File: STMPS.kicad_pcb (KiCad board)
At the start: 2 copper layers, 0 parts

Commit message: Fix jumper names for steppers. Start prepping for layout.
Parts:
- added C101: 100uf, Capacitors_SMD:c_elec_6.3x5.8, F.Cu at (163.1, 123.8)
- added C102: 10uf, Capacitors_SMD:C_0805_HandSoldering, F.Cu at (229.9, 94.0)
- added C103: 20pf, Capacitors_SMD:C_0805_HandSoldering, F.Cu at (226.2, 87.6)
- added C104: 20pf, Capacitors_SMD:C_0805_HandSoldering, F.Cu at (204.3, 107.7)
- added C105: 100nf, Capacitors_SMD:C_0805_HandSoldering, F.Cu at (185.7, 64.9)
- added C106: 100nf, Capacitors_SMD:C_0805_HandSoldering, F.Cu at (185.7, 63.0)
- added C107: 100nf, Capacitors_SMD:C_0805_HandSoldering, F.Cu at (185.7, 61.2)
- added C108: 100nf, Capacitors_SMD:C_0805_HandSoldering, F.Cu at (194.9, 53.1)
- added C109: 1uf, Capacitors_SMD:C_0805_HandSoldering, F.Cu at (203.6, 44.8)
- added C110: 100nf, Capacitors_SMD:C_0805_HandSoldering, F.Cu at (198.4, 67.8)
- added C111: 100nf, Capacitors_SMD:C_0805_HandSoldering, F.Cu at (193.0, 71.1)
- added C112: 100nf, Capacitors_SMD:C_0805_HandSoldering, F.Cu at (191.0, 66.6)
- added C113: 4.7uf, Capacitors_SMD:C_0805_HandSoldering, F.Cu at (205.2, 52.9)
- added C114: 4.7uf, Capacitors_SMD:C_0805_HandSoldering, F.Cu at (198.8, 59.5)
- added C115: 0.1uf, Capacitors_SMD:C_0805_HandSoldering, F.Cu at (192.3, 122.1)
- added C116: 10uf, Capacitors_SMD:C_0805_HandSoldering, F.Cu at (219.4, 94.0)
- added C117: 10uf, Capacitors_SMD:C_0805_HandSoldering, F.Cu at (210.8, 100.6)
- added C118: 0.1uf, Capacitors_SMD:C_0805_HandSoldering, F.Cu at (187.2, 122.1)
- added C201: 0.1uf, Capacitors_SMD:C_0805_HandSoldering, F.Cu at (163.8, 181.4)
- added C202: 0.1uf, Capacitors_SMD:C_0805_HandSoldering, F.Cu at (179.6, 181.6)
- added C203: 100uf, Capacitors_SMD:c_elec_6.3x5.8, F.Cu at (179.1, 172.9)
- added C301: 0.1uf, Capacitors_SMD:C_0805_HandSoldering, F.Cu at (227.3, 157.0)
- added C302: 0.1uf, Capacitors_SMD:C_0805_HandSoldering, F.Cu at (239.6, 139.5)
- added C303: 100uf, Capacitors_SMD:c_elec_6.3x5.8, F.Cu at (231.9, 141.8)
- added C401: 0.1uf, Capacitors_SMD:C_0805_HandSoldering, F.Cu at (329.5, 87.6)
- added C402: 0.1uf, Capacitors_SMD:C_0805_HandSoldering, F.Cu at (317.1, 105.1)
- added C403: 100uf, Capacitors_SMD:c_elec_6.3x5.8, F.Cu at (321.8, 90.0)
- added C501: 0.1uf, Capacitors_SMD:C_0805_HandSoldering, F.Cu at (221.7, 177.7)
- added C502: 0.1uf, Capacitors_SMD:C_0805_HandSoldering, F.Cu at (216.6, 177.7)
- added C503: 100uf, Capacitors_SMD:c_elec_6.3x5.8, F.Cu at (231.9, 169.1)
- added D101: 12v_PWR, LEDs:LED_0805, F.Cu at (181.0, 121.1)
- added D102: 3v_PWR, LEDs:LED_0805, F.Cu at (203.4, 120.1)
- added D601: D_Schottky_Small, Diodes_SMD:SOD-123, F.Cu at (244.1, 118.5)
- added D701: r, LEDs:LED_0805, F.Cu at (187.2, 139.1)
- added D801: r, LEDs:LED_0805, F.Cu at (277.1, 87.3)
- added JP101: JUMPER, stmps:MADW__SMD-solder-bridge-narrow, F.Cu at (179.9, 103.6)
- added JP201: MS3, stmps:MADW__SMD-solder-bridge-narrow, F.Cu at (154.3, 185.9)
- added JP202: MS2, stmps:MADW__SMD-solder-bridge-narrow, F.Cu at (167.0, 169.9)
- added JP203: MS1, stmps:MADW__SMD-solder-bridge-narrow, F.Cu at (167.0, 175.4)
- added JP301: MS3, stmps:MADW__SMD-solder-bridge-narrow, F.Cu at (219.8, 144.3)
- added JP302: MS2, stmps:MADW__SMD-solder-bridge-narrow, F.Cu at (219.8, 138.9)
- added JP303: MS1, stmps:MADW__SMD-solder-bridge-narrow, F.Cu at (207.0, 154.8)
- added JP401: MS3, stmps:MADW__SMD-solder-bridge-narrow, F.Cu at (296.9, 103.0)
- added JP402: MS2, stmps:MADW__SMD-solder-bridge-narrow, F.Cu at (309.7, 92.4)
- added JP403: MS1, stmps:MADW__SMD-solder-bridge-narrow, F.Cu at (309.7, 87.0)
- added JP501: MS3, stmps:MADW__SMD-solder-bridge-narrow, F.Cu at (207.0, 182.1)
- added JP502: MS2, stmps:MADW__SMD-solder-bridge-narrow, F.Cu at (219.8, 166.2)
- added JP503: MS1, stmps:MADW__SMD-solder-bridge-narrow, F.Cu at (219.8, 171.6)
- added P101: 12v IN, stmps:5EHDRC_1x04, F.Cu at (158.6, 99.5)
- added P102: 12v, Pin_Headers:Pin_Header_Straight_2x03, F.Cu at (172.1, 107.2)
- added P103: USB_OTG, Connect:USB_Micro-B, F.Cu at (182.3, 112.3)
- added P104: E0_THERM, Pin_Headers:Pin_Header_Straight_1x02, F.Cu at (198.1, 90.6)
- added P105: X_STOP, Pin_Headers:Pin_Header_Straight_1x03, F.Cu at (154.9, 111.1)
- added P106: SWD, Pin_Headers:Pin_Header_Straight_1x06, F.Cu at (149.6, 111.1)
- added P107: BED_THERM, Pin_Headers:Pin_Header_Straight_1x02, F.Cu at (172.8, 120.6)
- added P108: Y_STOP, Pin_Headers:Pin_Header_Straight_1x03, F.Cu at (161.0, 111.1)
- added P109: Z_STOP, Pin_Headers:Pin_Header_Straight_1x03, F.Cu at (154.9, 124.5)
- added P201: MOT, Pin_Headers:Pin_Header_Straight_1x04, F.Cu at (149.6, 173.5)
- added P301: MOT, Pin_Headers:Pin_Header_Straight_1x04, F.Cu at (202.3, 142.5)
- added P401: MOT, Pin_Headers:Pin_Header_Straight_1x04, F.Cu at (292.2, 90.6)
- added P501: MOT, Pin_Headers:Pin_Header_Straight_1x04, F.Cu at (202.3, 169.8)
- added P601: LP_OUT, Pin_Headers:Pin_Header_Straight_1x02, F.Cu at (254.0, 121.6)
- added P701: OUT, stmps:TB-1x02, F.Cu at (157.8, 149.7)
- added P801: OUT, stmps:TB-1x02, F.Cu at (247.7, 97.8)
- added Q601: SSM3K333, TO_SOT_Packages_SMD:SOT-23_Handsoldering, F.Cu at (241.5, 126.6)
- added Q701: IPP039N04L, TO_SOT_Packages_THT:TO-220_Neutral123_Vertical, F.Cu at (174.0, 142.5)
- added Q801: IPP039N04L, TO_SOT_Packages_THT:TO-220_Neutral123_Vertical, F.Cu at (263.8, 90.6)
- added R101: 560, Resistors_SMD:R_0805_HandSoldering, F.Cu at (231.4, 87.6)
- added R102: 56, Resistors_SMD:R_0805_HandSoldering, F.Cu at (197.6, 120.5)
- added R103: 220, Resistors_SMD:R_0805_HandSoldering, F.Cu at (224.7, 94.0)
- added R104: 100k, Resistors_SMD:R_0805_HandSoldering, F.Cu at (190.6, 128.5)
- added R105: 4.7k, Resistors_SMD:R_0805_HandSoldering, F.Cu at (180.1, 127.1)
- added R106: 4.7k, Resistors_SMD:R_0805_HandSoldering, F.Cu at (221.2, 100.4)
- added R107: 4.7k, Resistors_SMD:R_0805_HandSoldering, F.Cu at (214.7, 107.0)
- added R108: 4.7k, Resistors_SMD:R_0805_HandSoldering, F.Cu at (206.9, 114.1)
- added R201: 20k, Resistors_SMD:R_0805_HandSoldering, F.Cu at (169.0, 181.4)
- added R202: 100k, Resistors_SMD:R_0805_HandSoldering, F.Cu at (163.9, 187.8)
- added R203: 100k, Resistors_SMD:R_0805_HandSoldering, F.Cu at (174.4, 181.6)
- added R204: 0.05, Resistors_SMD:R_0805_HandSoldering, F.Cu at (186.9, 170.5)
- added R205: 0.05, Resistors_SMD:R_0805_HandSoldering, F.Cu at (169.2, 188.0)
- added R301: 20k, Resistors_SMD:R_0805_HandSoldering, F.Cu at (227.4, 150.6)
- added R302: 100k, Resistors_SMD:R_0805_HandSoldering, F.Cu at (216.7, 156.8)
- added R303: 100k, Resistors_SMD:R_0805_HandSoldering, F.Cu at (222.0, 150.4)
- added R304: 0.05, Resistors_SMD:R_0805_HandSoldering, F.Cu at (216.7, 150.4)
- added R305: 0.05, Resistors_SMD:R_0805_HandSoldering, F.Cu at (222.0, 156.8)
- added R401: 20k, Resistors_SMD:R_0805_HandSoldering, F.Cu at (311.9, 104.9)
- added R402: 100k, Resistors_SMD:R_0805_HandSoldering, F.Cu at (317.2, 98.7)
- added R403: 100k, Resistors_SMD:R_0805_HandSoldering, F.Cu at (306.5, 104.9)
- added R404: 0.05, Resistors_SMD:R_0805_HandSoldering, F.Cu at (306.5, 98.5)
- added R405: 0.05, Resistors_SMD:R_0805_HandSoldering, F.Cu at (311.9, 98.5)
- added R501: 20k, Resistors_SMD:R_0805_HandSoldering, F.Cu at (216.7, 184.1)
- added R502: 100k, Resistors_SMD:R_0805_HandSoldering, F.Cu at (227.0, 177.9)
- added R503: 100k, Resistors_SMD:R_0805_HandSoldering, F.Cu at (239.7, 166.8)
- added R504: 0.05, Resistors_SMD:R_0805_HandSoldering, F.Cu at (222.0, 184.3)
- added R505: 0.05, Resistors_SMD:R_0805_HandSoldering, F.Cu at (232.3, 177.9)
- added R601: 100k, Resistors_SMD:R_0805_HandSoldering, F.Cu at (259.7, 118.6)
- added R701: 100k, Resistors_SMD:R_0805_HandSoldering, F.Cu at (171.0, 150.6)
- added R702: 100, Resistors_SMD:R_0805_HandSoldering, F.Cu at (182.3, 139.5)
- added R703: 560, Resistors_SMD:R_0805_HandSoldering, F.Cu at (171.0, 157.0)
- added R801: 100k, Resistors_SMD:R_0805_HandSoldering, F.Cu at (260.9, 98.7)
- added R802: 100, Resistors_SMD:R_0805_HandSoldering, F.Cu at (260.9, 105.1)
- added R803: 560, Resistors_SMD:R_0805_HandSoldering, F.Cu at (272.2, 87.6)
- added RV201: 100k, stmps:BOURNS-TC33X-2, F.Cu at (186.8, 176.5)
- added RV301: 100k, stmps:BOURNS-TC33X-2, F.Cu at (232.6, 150.1)
- added RV401: 100k, stmps:BOURNS-TC33X-2, F.Cu at (322.5, 98.2)
- added RV501: 100k, stmps:BOURNS-TC33X-2, F.Cu at (239.6, 172.7)
- added SW101: RST, Buttons_Switches_ThroughHole:SW_PUSH_SMALL, F.Cu at (207.0, 88.5)
- added U101: AOZ8904, TO_SOT_Packages_SMD:SOT-23-6_Handsoldering, F.Cu at (171.9, 129.3)
- added U102: LM1117-3.3v, TO_SOT_Packages_SMD:TO-252-2Lead, F.Cu at (188.7, 95.9)
- added U103: STM32F411RCTx, Housings_QFP:LQFP-64_10x10mm_Pitch0.5mm, F.Cu at (173.0, 70.6)
- added U104: M24C04, Housings_SOIC:SOIC-8_3.9x4.9mm_Pitch1.27mm, F.Cu at (199.0, 99.9)
- added U201: A5984, stmps:TSSOP-24_4.4x7.8mm_Pitch0.65mm, F.Cu at (156.0, 173.4)
- added U301: A5984, stmps:TSSOP-24_4.4x7.8mm_Pitch0.65mm, F.Cu at (208.7, 142.3)
- added U401: A5984, stmps:TSSOP-24_4.4x7.8mm_Pitch0.65mm, F.Cu at (298.6, 90.5)
- added U501: A5984, stmps:TSSOP-24_4.4x7.8mm_Pitch0.65mm, F.Cu at (208.7, 169.6)
- added W101: TEST_1P, Connect:PINTST, F.Cu at (190.5, 110.2)
- added W102: TEST_1P, Connect:PINTST, F.Cu at (206.4, 95.0)
- added W103: TEST_1P, Connect:PINTST, F.Cu at (198.4, 106.8)
- added W104: TEST_1P, Connect:PINTST, F.Cu at (215.1, 86.8)
- added Y101: Crystal, Crystals:Crystal_HC49-U_Vertical, F.Cu at (189.1, 102.9)

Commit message: Complete routing, first pass.
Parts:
- removed C115: 0.1uf, Capacitors_SMD:C_0805_HandSoldering
- removed SW101: RST, Buttons_Switches_ThroughHole:SW_PUSH_SMALL
- removed W101, W102, W103, W104: TEST_1P, Connect:PINTST
- added C204: 0.1uf, Capacitors_SMD:C_0805_HandSoldering, F.Cu at (166.9, 126.4)
- added C304: 0.1uf, Capacitors_SMD:C_0805_HandSoldering, F.Cu at (166.6, 143.8)
- added C404: 0.1uf, Capacitors_SMD:C_0805_HandSoldering, F.Cu at (197.6, 126.5)
- added C504: 0.1uf, Capacitors_SMD:C_0805_HandSoldering, F.Cu at (197.6, 143.7)
- C102, C105, C106, C107, C108, C109, C110, C111, C112, C113, C114, R104, R701, R702, R801, R802, U102: moved to B.Cu
- JP101: value JUMPER -> BOOT0; footprint stmps:MADW__SMD-solder-bridge-narrow -> Pin_Headers:Pin_Header_Straight_1x02_Pitch2.00mm
- P701, P801: footprint stmps:TB-1x02 -> Connectors_Molex:Molex_KK-6410-02_02x2.54mm_Straight
- moved C403 171.3 mm to (153.0, 119.4), turned to 90 degrees
- moved C401 170.7 mm to (161.3, 117.0), turned to 270 degrees
- moved RV401 165.2 mm to (159.8, 127.1), turned to 270 degrees
- moved R402 158.8 mm to (159.5, 117.0), turned to 270 degrees
- moved R401 157.8 mm to (155.7, 127.1), turned to 90 degrees
- moved JP402 152.0 mm to (160.4, 120.9), turned to 270 degrees
- moved JP403 151.9 mm to (161.6, 120.9), turned to 270 degrees
- moved C402 150.7 mm to (166.9, 115.9)
- moved R403 147.8 mm to (159.9, 123.6), turned to 180 degrees
- moved R405 139.9 mm to (174.1, 122.8)
- moved JP401 139.0 mm to (159.1, 120.9), turned to 270 degrees
- moved U401 135.3 mm to (166.9, 121.1)
- moved R404 134.1 mm to (174.1, 119.5)
- moved P401 118.5 mm to (178.8, 124.8), turned to 180 degrees
- moved C109 106.9 mm to (141.4, 131.7)
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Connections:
- net Net-(C102-Pad1) renamed /+5v
- U101 pad 1: Net-(U101-Pad1) -> /USB_DP
- U101 pad 3: Net-(U101-Pad3) -> /USB_DN
- U101 pad 4: /USB_DN -> Net-(U101-Pad4)
- U101 pad 6: /USB_DP -> Net-(U101-Pad6)
- U103 pad 33: /E0_Stepper/ENABLE -> /E0_Stepper/STEP
- U103 pad 34: /E0_Stepper/STEP -> /E0_Stepper/DIR
- U103 pad 35: /E0_Stepper/DIR -> /E0_Stepper/ENABLE
- U201 pad 15: Net-(P201-Pad2) -> Net-(P201-Pad1)
- U201 pad 18: Net-(P201-Pad1) -> Net-(P201-Pad2)
- U201 pad T: (no net) -> GND
- U301 pad 15: Net-(P301-Pad2) -> Net-(P301-Pad1)
- U301 pad 18: Net-(P301-Pad1) -> Net-(P301-Pad2)
- U301 pad T: (no net) -> GND
- U401 pad 15: Net-(P401-Pad2) -> Net-(P401-Pad1)
- U401 pad 18: Net-(P401-Pad1) -> Net-(P401-Pad2)
- U401 pad T: (no net) -> GND
- U501 pad 15: Net-(P501-Pad2) -> Net-(P501-Pad1)
- U501 pad 18: Net-(P501-Pad1) -> Net-(P501-Pad2)
- U501 pad T: (no net) -> GND
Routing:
- net +3.3v: track 0.00 -> 248.6 mm, vias 0 -> 9
- net GND: track 0.00 -> 147.1 mm, vias 0 -> 60
- net /BED_FET/PWM_IN: track 0.00 -> 97.7 mm, vias 0 -> 3
- net /E0_FET/PWM_IN: track 0.00 -> 79.3 mm, vias 0 -> 3
- net /Fan_FET/PWM_IN: track 0.00 -> 78.8 mm, vias 0 -> 2
- net /X_Stepper/DIR: track 0.00 -> 74.3 mm, vias 0 -> 2
- net /X_Stepper/ENABLE: track 0.00 -> 71.6 mm, vias 0 -> 3
- net /X_Stepper/STEP: track 0.00 -> 70.2 mm, vias 0 -> 2
- net /E0_Stepper/ENABLE: track 0.00 -> 62.0 mm, vias 0 -> 3
- net /E0_Stepper/DIR: track 0.00 -> 57.0 mm, vias 0 -> 2
- net /E0_Stepper/STEP: track 0.00 -> 53.8 mm, vias 0 -> 2
- net /NRST: track 0.00 -> 51.0 mm, vias 0 -> 1
- net /Y_Stepper/DIR: track 0.00 -> 39.3 mm, vias 0 -> 2
- net /Y_Stepper/STEP: track 0.00 -> 36.7 mm, vias 0 -> 2
- net /Y_Stepper/ENABLE: track 0.00 -> 35.5 mm, vias 0 -> 3
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- added copper zone on F.Cu, net +12v
- added copper zone on B.Cu, net GND
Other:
- board outline added: 98.3 x 37.3 mm
- net class Default: via_dia 0.6858 -> 0.7112
- net class Low-Power added: clearance 0.1524, trace_width 0.254, via_dia 0.7112, via_drill 0.3302
- net class Power: clearance 0.254 -> 0.1524; trace_width 0.6096 -> 0.8128; via_dia 0.889 -> 0.7112; via_drill 0.4572 -> 0.3302

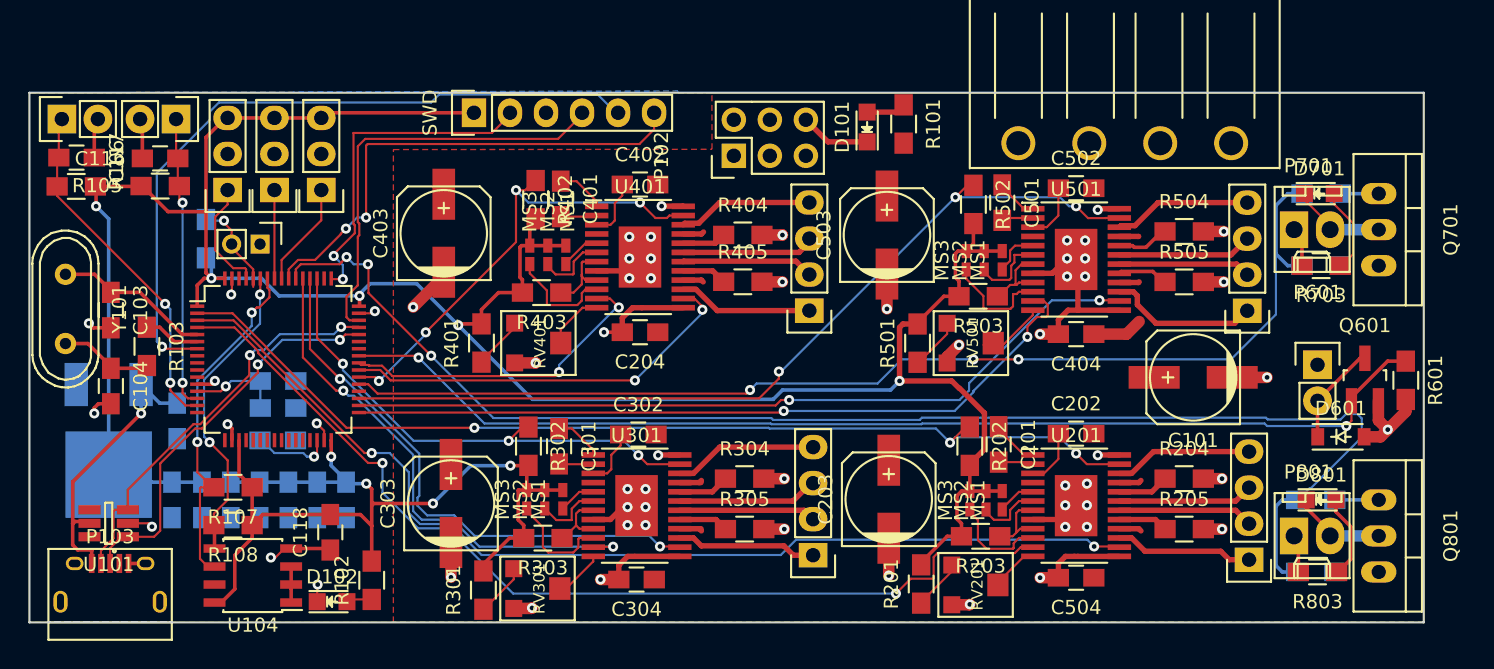
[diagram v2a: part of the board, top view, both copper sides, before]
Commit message: Cleanup silkscreen and other minor tweaks.
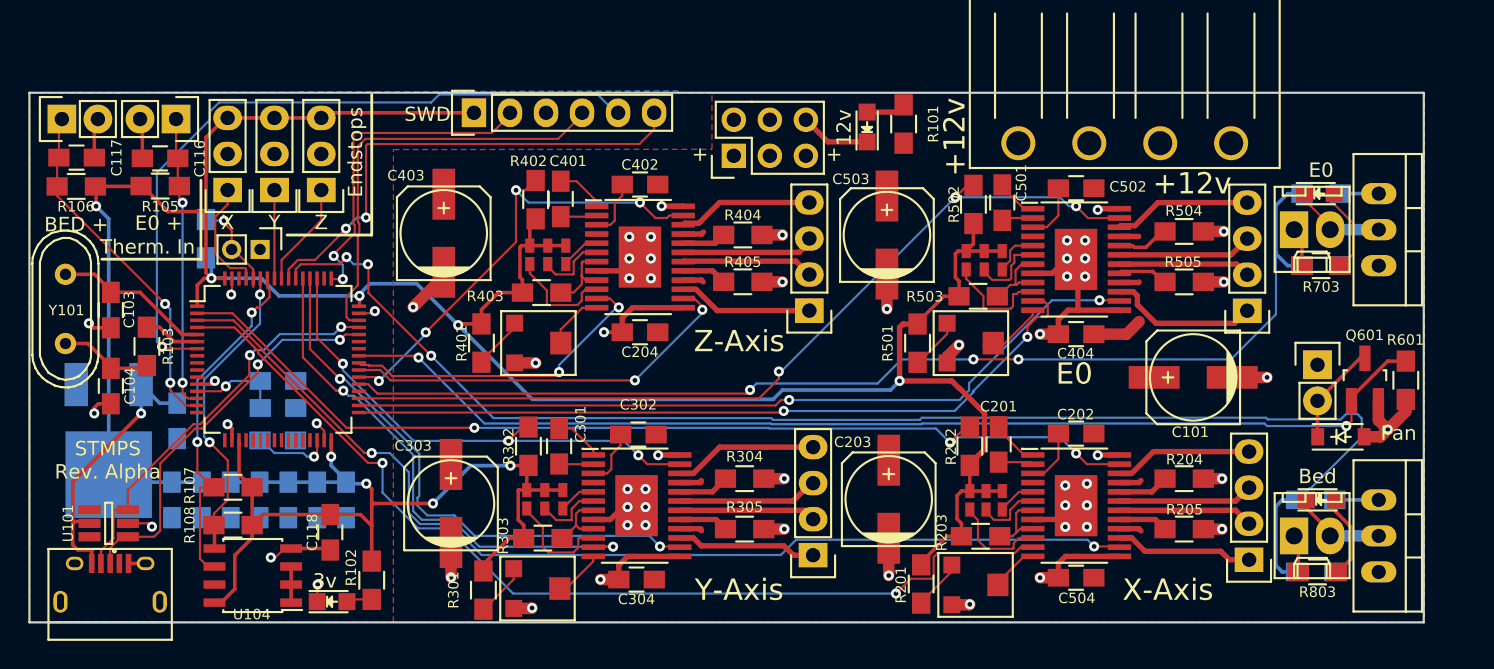
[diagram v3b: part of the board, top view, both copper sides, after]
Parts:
- added REF**: Symbol_OSHW-Logo_SilkScreen, Symbols:Symbol_OSHW-Logo_SilkScreen, B.Cu at (130.3, 118.1)
- JP503: value MS1 -> eMS1
- moved JP101 0.38 mm to (140.1, 120.5)
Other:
- board text added: "+"
- board text added: "+12v"
- board text added: "12v"
- board text added: "3v"
- board text added: "BED +"
- board text added: "Bed"
- board text added: "E0"
- board text added: "E0 +"
- board text added: "Endstops"
- board text added: "Fan"
- board text added: "STMPS Rev. Alpha"
- board text added: "Therm. In"
- board text added: "X"
- board text added: "X-Axis"
- board text added: "Y"
- board text added: "Y-Axis"
- board text added: "Z"
- board text added: "Z-Axis"

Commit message: Finalized layout for Alpha 1.
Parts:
- JP503: value eMS1 -> MS1
- R201, R301, R401, R501: value 20k -> 200k
- R204, R205, R304, R305, R404, R405, R504, R505: value 0.05 -> 0.1
- moved REF** 1.78 mm to (130.3, 116.3), turned to 180 degrees
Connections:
- R201 pad 2: +3.3v -> +12v
- R301 pad 2: +3.3v -> +12v
- R401 pad 2: +3.3v -> +12v
- R501 pad 2: +3.3v -> +12v
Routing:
- net +3.3v: track 248.6 -> 240.4 mm
- net +12v: track 21.7 -> 22.3 mm

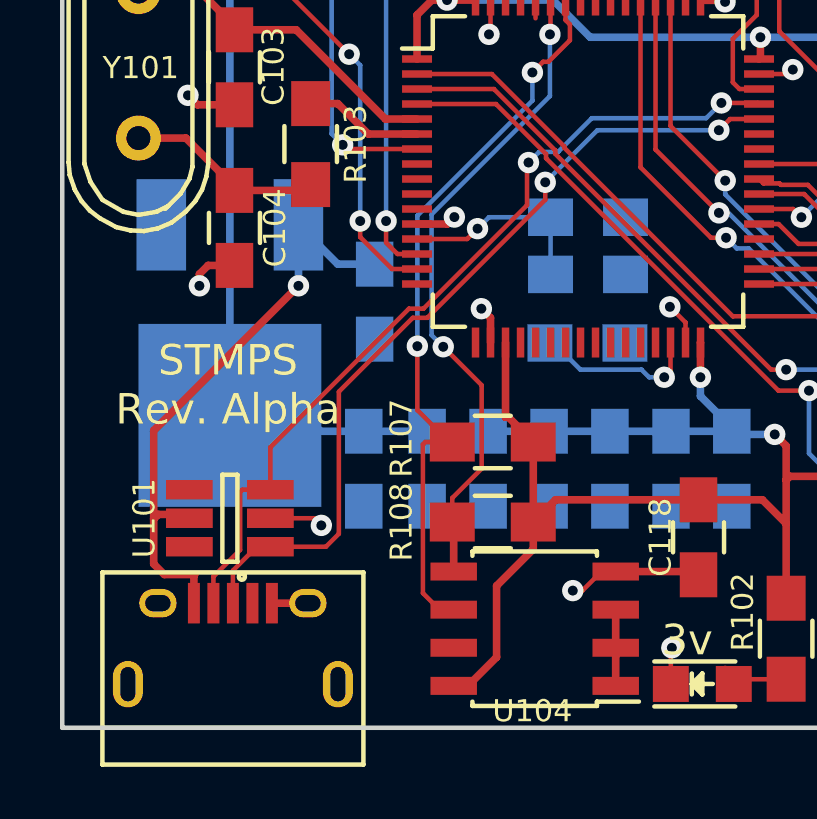
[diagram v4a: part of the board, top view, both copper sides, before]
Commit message: Fix USB connection. Cleanups.
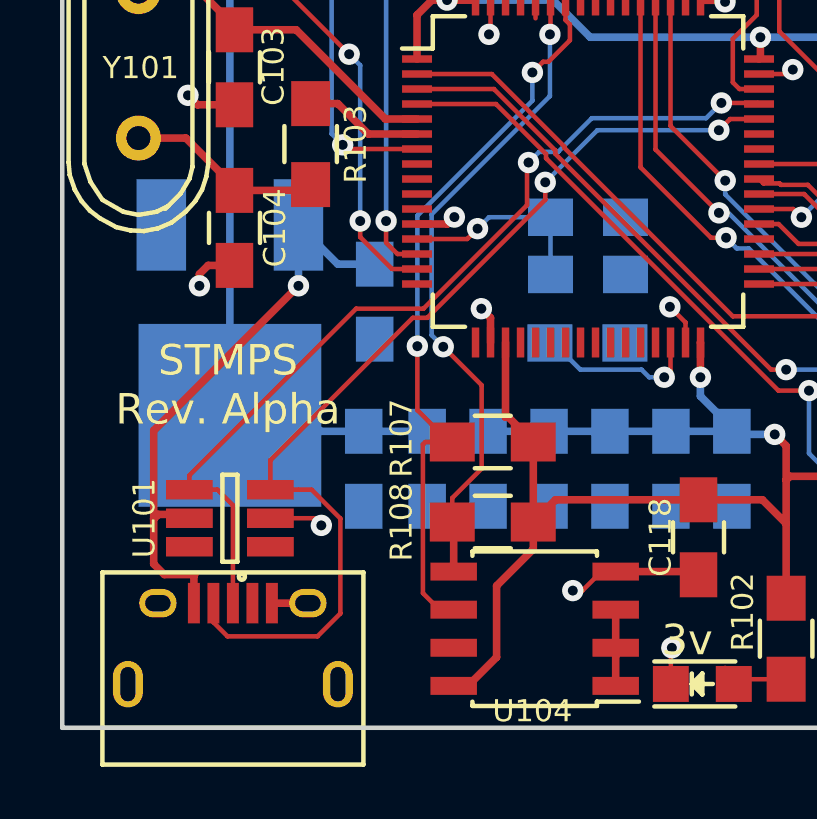
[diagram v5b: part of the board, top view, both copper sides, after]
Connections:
- P103 pad 2: /USB_DN -> /USB_DM
- U101 pad 1: /USB_DP -> Net-(U101-Pad1)
- U101 pad 3: /USB_DN -> /USB_DM
- U101 pad 4: Net-(U101-Pad4) -> /USB_DP
- U103 pad 44: /USB_DP -> /USB_DM
- U103 pad 45: /USB_DN -> /USB_DP
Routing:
- net /USB_DM: track 0.00 -> 33.6 mm, vias 0 -> 2
- net /USB_DN: track 28.4 -> 0.00 mm, vias 2 -> 0
- net /USB_DP: track 28.0 -> 30.4 mm

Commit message: WIP rev B.
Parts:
- removed C118: 0.1uf, Capacitors_SMD:C_0805_HandSoldering
- removed R107, R108: 4.7k, Resistors_SMD:R_0805_HandSoldering
- removed REF**: Symbol_OSHW-Logo_SilkScreen, Symbols:Symbol_OSHW-Logo_SilkScreen
- removed U104: M24C04, Housings_SOIC:SOIC-8_3.9x4.9mm_Pitch1.27mm
- added D103: D_Schottky_Small, Diodes_SMD:SOD-123, F.Cu at (150.4, 182.8)
- added U105: CHIP-TOP, stmps:CHIP-MIN, F.Cu at (47.8, 79.8)
- C103, C104, D701, D801, R103, R703, R803: moved to B.Cu
- moved Q701 91.6 mm to (127.4, 115.3), turned to 90 degrees
- moved D601 89.0 mm to (127.4, 128.8)
- moved R601 89.0 mm to (132.0, 124.8)
- moved P601 89.0 mm to (125.7, 123.7)
- moved Q601 89.0 mm to (129.1, 124.7)
- moved R702 88.2 mm to (126.7, 120.4), turned to 0 degrees
- moved R701 84.8 mm to (130.2, 118.9), turned to 90 degrees
- moved D701 84.6 mm to (130.2, 114.3), turned to 90 degrees
- moved Q801 83.1 mm to (139.7, 115.7), turned to 90 degrees
- moved R703 81.8 mm to (133.5, 113.3), turned to 0 degrees
- moved P701 77.9 mm to (135.1, 116.3), turned to 180 degrees
- moved R802 77.4 mm to (139.2, 120.4), turned to 0 degrees
- moved D801 76.2 mm to (142.5, 114.3), turned to 90 degrees
- moved R801 76.0 mm to (142.5, 118.9), turned to 90 degrees
- moved P301 75.7 mm to (105.9, 122.7), turned to 270 degrees
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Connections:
- U103 pad 10: Net-(U103-Pad10) -> /E0_Stepper/ENABLE
- U103 pad 33: /E0_Stepper/STEP -> Net-(U103-Pad33)
- U103 pad 34: /E0_Stepper/DIR -> /Z_Stepper/DIR
- U103 pad 35: /E0_Stepper/ENABLE -> /Z_Stepper/STEP
- U103 pad 36: Net-(U103-Pad36) -> /Z_Stepper/ENABLE
- U103 pad 38: /Z_Stepper/ENABLE -> /Y_Stepper/DIR
- U103 pad 39: /Z_Stepper/DIR -> /Y_Stepper/STEP
- U103 pad 40: /Z_Stepper/STEP -> /Y_Stepper/ENABLE
- U103 pad 42: Net-(U103-Pad42) -> /USART1_TX
- U103 pad 43: Net-(U103-Pad43) -> /USART1_RX
- U103 pad 51: /Y_Stepper/ENABLE -> Net-(U103-Pad51)
- U103 pad 52: /Y_Stepper/DIR -> Net-(U103-Pad52)
- U103 pad 53: /Y_Stepper/STEP -> Net-(U103-Pad53)
- U103 pad 62: Net-(U103-Pad62) -> /CHIP_1_WIRE
- U103 pad 8: Net-(U103-Pad8) -> /E0_Stepper/STEP
- U103 pad 9: Net-(U103-Pad9) -> /E0_Stepper/DIR
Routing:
- net +3.3v: track 240.4 -> 39.9 mm, vias 9 -> 4
- net GND: track 147.1 -> 16.5 mm, vias 60 -> 3
- net /BED_FET/PWM_IN: track 97.7 -> 0.00 mm, vias 3 -> 0
- net /E0_FET/PWM_IN: track 79.3 -> 0.00 mm, vias 3 -> 0
- net /Fan_FET/PWM_IN: track 78.8 -> 0.00 mm, vias 2 -> 0
- net /X_Stepper/DIR: track 74.3 -> 0.00 mm, vias 2 -> 0
- net /X_Stepper/ENABLE: track 71.6 -> 0.00 mm, vias 3 -> 0
- net /X_Stepper/STEP: track 70.2 -> 0.00 mm, vias 2 -> 0
- net /E0_Stepper/ENABLE: track 62.0 -> 0.00 mm, vias 3 -> 0
- net /E0_Stepper/DIR: track 57.0 -> 0.00 mm, vias 2 -> 0
- net /E0_Stepper/STEP: track 53.8 -> 0.00 mm, vias 2 -> 0
- net /NRST: track 51.0 -> 0.00 mm, vias 1 -> 0
- net /SWO: track 34.7 -> 0.00 mm, vias 2 -> 0
- net /USB_DM: track 33.6 -> 0.00 mm, vias 2 -> 0
- net /USB_DP: track 30.4 -> 0.00 mm, vias 2 -> 0
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- removed copper zone on B.Cu, net GND
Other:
- board size 98.3 x 37.3 mm -> 85.9 x 56.9 mm
